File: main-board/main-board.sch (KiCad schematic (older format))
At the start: 54 parts, among them J1 MOTOR0, J10 PROGRAMMER, J11 CAM0, J12 CAM1, J13 CAM2, J14 CAM3, J15 CAM4, J16 CAM5, J17 CAM6, J18 CAM7, J2 MOTOR1, J3 MOTOR2, J4 MOTOR3, J5 RJ45, J6 MOTOR4, J7 MOTOR5, J8 MOTOR6, J9 MOTOR7, SW1 SW_SPST, T1 ATB2012E-50011M-T01, T2 ATB2012E-50011M-T01, U1 MCP2515-EST, U2 ATA6560, U3 ATmega2560-16AU | Main Proc, U4 MC14051B, U5 MC14051B, U6 SN75HVD3082EDR, U7 LTC1983ES6-5-TRPBF, U8 OPAMP, U9 OPAMP, Y1 20MHz, Y2 20MHz

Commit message: begin board
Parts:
- added J19: PowerBoard Interface, Connector_JST:JST_EH_B04B-EH-A_1x04_P2.50mm_Vertical, symbol Connector:Conn_01x04_Male
- added J20: IMU Breakout, Connector_JST:JST_EH_B04B-EH-A_1x04_P2.50mm_Vertical, symbol Connector:Conn_01x04_Male
- C1, C2, C3, C4, C5, C6, C7, C8, C9: footprint (none) -> Capacitor_SMD:C_0603_1608Metric
- D1: footprint (none) -> Diode_SMD:D_0603_1608Metric
- D2: footprint SOT-23-3 -> Package_TO_SOT_SMD:SOT-23
- J1, J2, J3, J4, J6, J7, J8, J9: footprint (none) -> Connector_JST:JST_EH_B03B-EH-A_1x03_P2.50mm_Vertical
- J10: footprint (none) -> Connector_JST:JST_EH_B05B-EH-A_1x05_P2.50mm_Vertical
- J11, J12, J13, J14, J15, J16, J17, J18: footprint (none) -> Connector_PinSocket_2.54mm:PinSocket_2x03_P2.54mm_Vertical
- J5: footprint (none) -> Connector_RJ:RJ45_Amphenol_54602-x08_Horizontal
- R1, R10, R11, R2, R3, R4, R5, R6, R7, R8, R9: footprint (none) -> Resistor_SMD:R_0603_1608Metric
- SW1: footprint (none) -> Button_Switch_THT:SW_Tactile_Straight_KSA0Axx1LFTR
- T1, T2: footprint XFMR_ATB2012E-50011M-T01 -> HHM1595A1:BALUN_HHM1595A1
- U2: footprint (none) -> Package_SO:SOIC-8_3.9x4.9mm_P1.27mm
- U4, U5: footprint (none) -> Package_SO:SOIC-16_3.9x9.9mm_P1.27mm
- U6: footprint D8 -> Package_SO:SOIC-8_3.9x4.9mm_P1.27mm
- U7: footprint SOT-23_S6 -> Package_TO_SOT_SMD:SOT-23-6
- U8, U9: footprint (none) -> Package_TO_SOT_SMD:SOT-23-5
- Y1, Y2: footprint (none) -> Crystal:Crystal_HC49-U_Vertical
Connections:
- net labels added: +3V3, SCL, SDA
- wire segments 140 -> 141
- no-connect marks 67 -> 65

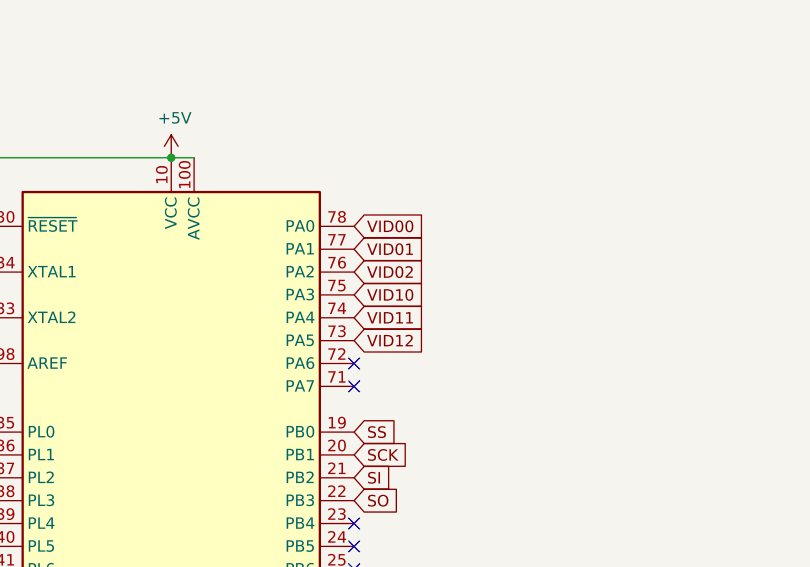
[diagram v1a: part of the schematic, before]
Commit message: add traces for all signals except cameras
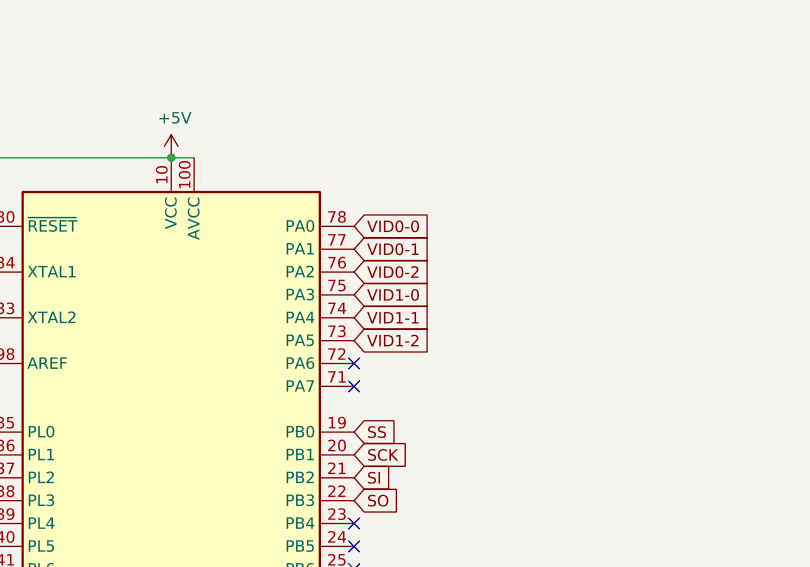
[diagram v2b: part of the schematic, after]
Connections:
- net labels removed: VID00, VID01, VID02, VID10, VID11, VID12
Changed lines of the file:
@@
 $EndComp
 Text GLabel 6300 1650 2    50   Input ~ 0
-VID00
+VID0-0
 Text GLabel 6300 1750 2    50   Input ~ 0
-VID01
+VID0-1
 Text GLabel 6300 1850 2    50   Input ~ 0
-VID02
+VID0-2
 Text GLabel 6300 1950 2    50   Input ~ 0
-VID10
+VID1-0
 Text GLabel 6300 2050 2    50   Input ~ 0
-VID11
+VID1-1
 Text GLabel 6300 2150 2    50   Input ~ 0
-VID12
+VID1-2
 Text GLabel 4700 6650 0    50   Input ~ 0
 M0

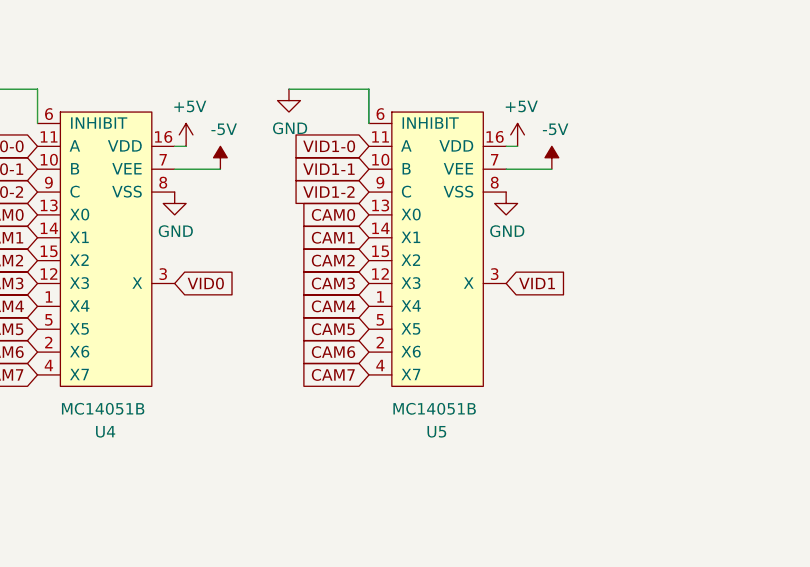
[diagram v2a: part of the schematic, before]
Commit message: complete electrical circuit, needs holes
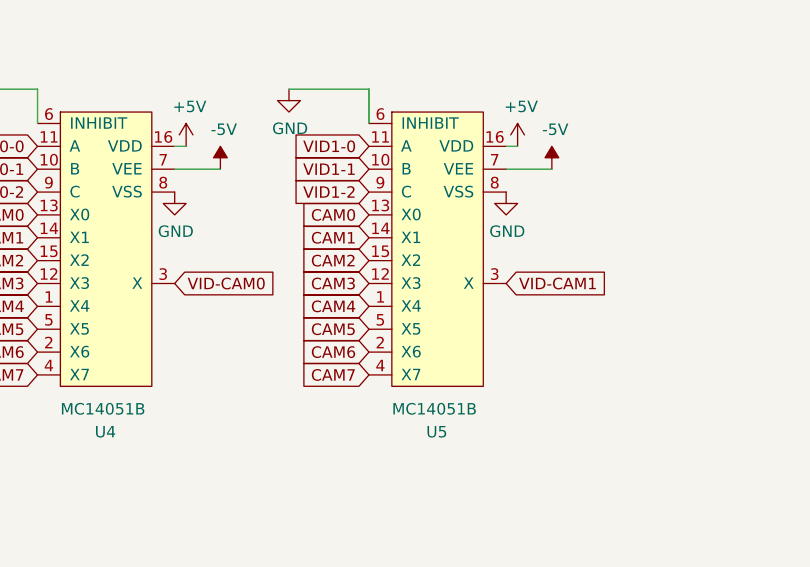
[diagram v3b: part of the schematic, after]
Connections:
- net labels removed: VID0, VID1
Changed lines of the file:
@@
 $EndComp
 Text GLabel 9650 3400 2    50   Input ~ 0
-VID0
+VID-CAM0
 Text GLabel 11100 3400 2    50   Input ~ 0
-VID1
+VID-CAM1
 $Comp
 L power:GND #PWR034

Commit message: Review+changes- see description
Schematic:
* add ICSP connector
* add VPP and diode D3for uC programming


PCB:
* add ICSP connector
* add VPP diode
* change tether connector from RJ45 to 2.54mm pitch 1x8 header
* slight silkscreen changes
* removed some overlapping vias
* moved vias from SMD pads
* slight changes to GND top copper pour



Requested before approval:
* silkscreen work
* Vinnie review


Requested other:
* Schematic formatting- boxes, labels, page layout, etc
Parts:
- added D3: D_x2_KCom_AAK, Package_TO_SOT_SMD:SOT-23, symbol Device:D_x2_KCom_AAK
- added J21: ICSP (DO NOT POPULATE), Connector_PinHeader_1.00mm:PinHeader_2x03_P1.00mm_Vertical, symbol Connector_Generic:Conn_02x03_Odd_Even
- D2: symbol CDSOT23-SM712:CDSOT23-SM712 -> main-board-rescue:CDSOT23-SM712-CDSOT23-SM712
- J5: footprint Connector_RJ:RJ45_Amphenol_54602-x08_Horizontal -> Connector_PinHeader_2.54mm:PinHeader_1x08_P2.54mm_Vertical
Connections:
- net labels added: RESET_MAIN, VPP
- wire segments 141 -> 151
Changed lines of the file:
@@
 F 0 "J5" V 8659 9330 50  0000 L CNN
 F 1 "RJ45" V 8750 9330 50  0000 L CNN
-F 2 "Connector_RJ:RJ45_Amphenol_54602-x08_Horizontal" V 8650 8825 50  0001 C CNN
+F 2 "Connector_PinHeader_2.54mm:PinHeader_1x08_P2.54mm_Vertical" V 8650 8825 50  0001 C CNN
 F 3 "~" V 8650 8825 50  0001 C CNN
 	1    8650 8800
@@
 L power:+5V #PWR012
 U 1 1 5BC811BE
-P 5500 1350
-F 0 "#PWR012" H 5500 1200 50  0001 C CNN
-F 1 "+5V" H 5515 1523 50  0000 C CNN
-F 2 "" H 5500 1350 50  0001 C CNN
-F 3 "" H 5500 1350 50  0001 C CNN
-	1    5500 1350
-	1    0    0    -1
-$EndComp
-Wire Wire Line
-	5500 1350 5600 1350
+P 5950 1050
+F 0 "#PWR012" H 5950 900 50  0001 C CNN
+F 1 "+5V" H 5965 1223 50  0000 C CNN
+F 2 "" H 5950 1050 50  0001 C CNN
+F 3 "" H 5950 1050 50  0001 C CNN
+	1    5950 1050
+	1    0    0    -1
+$EndComp
+Wire Wire Line
+	5500 1350 5550 1350
 Connection ~ 5500 1350
 $Comp
@@
 F 3 "" H 10650 8300 50  0001 C CNN
 	1    10650 8300
-	1    0    0    -1
-$EndComp
-$Comp
-L power:+5V #PWR039
-U 1 1 5BCA444A
-P 10650 7900
-F 0 "#PWR039" H 10650 7750 50  0001 C CNN
-F 1 "+5V" H 10665 8073 50  0000 C CNN
-F 2 "" H 10650 7900 50  0001 C CNN
-F 3 "" H 10650 7900 50  0001 C CNN
-	1    10650 7900
 	1    0    0    -1
 $EndComp
@@
 	3500 2200 3500 2300
 $Comp
-L CDSOT23-SM712:CDSOT23-SM712 D2
+L main-board-rescue:CDSOT23-SM712-CDSOT23-SM712 D2
 U 1 1 5BCEE3C3
 P 14800 1500
@@
 SDA
 NoConn ~ 6300 4750
+$Comp
+L Connector_Generic:Conn_02x03_Odd_Even J21
+U 1 1 5BD727D5
+P 10900 10000
+F 0 "J21" H 10950 10350 50  0000 C CNN
+F 1 "ICSP (DO NOT POPULATE)" H 10600 10250 50  0000 C CNN
+F 2 "Connector_PinHeader_1.00mm:PinHeader_2x03_P1.00mm_Vertical" H 10900 10000 50  0001 C CNN
+F 3 "~" H 10900 10000 50  0001 C CNN
+	1    10900 10000
+	1    0    0    -1
+$EndComp
+Text GLabel 10700 9900 0    50   Input ~ 0
+SO
+Text GLabel 11200 10000 2    50   Input ~ 0
+SI
+Text GLabel 10700 10000 0    50   Input ~ 0
+SCK
+Text GLabel 10700 10100 0    50   Input ~ 0
+RESET_MAIN
+$Comp
+L power:GND #PWR0105
+U 1 1 5BD754CF
+P 11250 10150
+F 0 "#PWR0105" H 11250 9900 50  0001 C CNN
+F 1 "GND" H 11255 9977 50  0000 C CNN
+F 2 "" H 11250 10150 50  0001 C CNN
+F 3 "" H 11250 10150 50  0001 C CNN
+	1    11250 10150
+	1    0    0    -1
+$EndComp
+Wire Wire Line
+	11250 10150 11250 10100
+Wire Wire Line
+	11250 10100 11200 10100
+Wire Wire Line
+	11200 9900 11250 9900
+Wire Wire Line
+	11250 9900 11250 9850
+$Comp
+L Device:D_x2_KCom_AAK D3
+U 1 1 5BD83587
+P 5550 1100
+F 0 "D3" H 5550 1316 50  0000 C CNN
+F 1 "D_x2_KCom_AAK" H 5550 1225 50  0000 C CNN
+F 2 "Package_TO_SOT_SMD:SOT-23" H 5550 1100 50  0001 C CNN
+F 3 "~" H 5550 1100 50  0001 C CNN
+	1    5550 1100
+	1    0    0    -1
+$EndComp
+Wire Wire Line
+	5950 1050 5950 1100
+Wire Wire Line
+	5950 1100 5850 1100
+$Comp
+L power:VPP #PWR0106
+U 1 1 5BD8A805
+P 5150 1050
+F 0 "#PWR0106" H 5150 900 50  0001 C CNN
+F 1 "VPP" H 5165 1223 50  0000 C CNN
+F 2 "" H 5150 1050 50  0001 C CNN
+F 3 "" H 5150 1050 50  0001 C CNN
+	1    5150 1050
+	1    0    0    -1
+$EndComp
+Wire Wire Line
+	5250 1100 5150 1100
+Wire Wire Line
+	5150 1100 5150 1050
+Wire Wire Line
+	5550 1300 5550 1350
+Connection ~ 5550 1350
+Wire Wire Line
+	5550 1350 5600 1350
+$Comp
+L power:VPP #PWR0107
+U 1 1 5BDA353F
+P 11250 9850
+F 0 "#PWR0107" H 11250 9700 50  0001 C CNN
+F 1 "VPP" H 11265 10023 50  0000 C CNN
+F 2 "" H 11250 9850 50  0001 C CNN
+F 3 "" H 11250 9850 50  0001 C CNN
+	1    11250 9850
+	1    0    0    -1
+$EndComp
+$Comp
+L power:VPP #PWR0108
+U 1 1 5BDA39A3
+P 10650 7900
+F 0 "#PWR0108" H 10650 7750 50  0001 C CNN
+F 1 "VPP" H 10665 8073 50  0000 C CNN
+F 2 "" H 10650 7900 50  0001 C CNN
+F 3 "" H 10650 7900 50  0001 C CNN
+	1    10650 7900
+	1    0    0    -1
+$EndComp
 $EndSCHEMATC

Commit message: Various changes (see description)
Schematic Changes:
* add optional second RS485
* add filter caps to IC power
* remove input resistor on reset line of 2560
* change CAN UART lines to be tx<>tx rx<>rx

PCB Changes:
* reorganize camera section
* add header labels
* minor fixes
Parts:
- removed C7: 10uF, Capacitor_SMD:C_0603_1608Metric, symbol Device:C_Small
- removed J11: CAM0, Connector_PinSocket_2.54mm:PinSocket_2x03_P2.54mm_Vertical, symbol Connector_Generic:Conn_02x03_Counter_Clockwise
- removed J12: CAM1, Connector_PinSocket_2.54mm:PinSocket_2x03_P2.54mm_Vertical, symbol Connector_Generic:Conn_02x03_Counter_Clockwise
- removed J13: CAM2, Connector_PinSocket_2.54mm:PinSocket_2x03_P2.54mm_Vertical, symbol Connector_Generic:Conn_02x03_Counter_Clockwise
- removed J14: CAM3, Connector_PinSocket_2.54mm:PinSocket_2x03_P2.54mm_Vertical, symbol Connector_Generic:Conn_02x03_Counter_Clockwise
- removed J15: CAM4, Connector_PinSocket_2.54mm:PinSocket_2x03_P2.54mm_Vertical, symbol Connector_Generic:Conn_02x03_Counter_Clockwise
- removed J16: CAM5, Connector_PinSocket_2.54mm:PinSocket_2x03_P2.54mm_Vertical, symbol Connector_Generic:Conn_02x03_Counter_Clockwise
- removed J17: CAM6, Connector_PinSocket_2.54mm:PinSocket_2x03_P2.54mm_Vertical, symbol Connector_Generic:Conn_02x03_Counter_Clockwise
- removed J18: CAM7, Connector_PinSocket_2.54mm:PinSocket_2x03_P2.54mm_Vertical, symbol Connector_Generic:Conn_02x03_Counter_Clockwise
- removed U8, U9: OPAMP, Package_TO_SOT_SMD:SOT-23-5, symbol pspice:OPAMP
- added C10, C11, C12, C13, C14, C15, C16, C17, C18, C19: 100nF, Capacitor_SMD:C_0603_1608Metric, symbol Device:C_Small
- added D4: CDSOT23-SM712, Package_TO_SOT_SMD:SOT-23, symbol main-board-rescue:CDSOT23-SM712-CDSOT23-SM712
- added J11: CAM0, symbol Connector_Generic:Conn_02x03_Odd_Even
- added J12: CAM1, symbol Connector_Generic:Conn_02x03_Odd_Even
- added J13: CAM2, symbol Connector_Generic:Conn_02x03_Odd_Even
- added J14: CAM3, symbol Connector_Generic:Conn_02x03_Odd_Even
- added J15: CAM4, symbol Connector_Generic:Conn_02x03_Odd_Even
- added J16: CAM5, symbol Connector_Generic:Conn_02x03_Odd_Even
- added J17: CAM6, symbol Connector_Generic:Conn_02x03_Odd_Even
- added J18: CAM7, symbol Connector_Generic:Conn_02x03_Odd_Even
- added R12: 10k, Resistor_SMD:R_0603_1608Metric, symbol Device:R_Small
- added R13, R14: 10, Resistor_SMD:R_0603_1608Metric, symbol Device:R_Small
- added R15, R16: 100, Resistor_SMD:R_0603_1608Metric, symbol Device:R_Small
- added U8: THS7314DR, ths7314dr:THS7314DR, symbol ths7314dr:THS7314DR
- added U9: SN75HVD3082EDR, Package_SO:SOIC-8_3.9x4.9mm_P1.27mm, symbol main-board-rescue:SN75HVD3082EDR-SN75HVD3082EDR_
- J1, J2, J3, J4, J6, J7, J8, J9: footprint Connector_JST:JST_EH_B03B-EH-A_1x03_P2.50mm_Vertical -> Connector_PinHeader_2.54mm:PinHeader_1x03_P2.54mm_Vertical
- J10: footprint Connector_JST:JST_EH_B05B-EH-A_1x05_P2.50mm_Vertical -> Connector_PinHeader_2.54mm:PinHeader_1x05_P2.54mm_Vertical
- J19, J20: footprint Connector_JST:JST_EH_B04B-EH-A_1x04_P2.50mm_Vertical -> Connector_PinHeader_2.54mm:PinHeader_1x04_P2.54mm_Vertical
- R5: value 100k -> 10k
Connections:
- net labels added: RS485+2, RS485-2
- wire segments 151 -> 200
- no-connect marks 65 -> 68
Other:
- note added: "SECOND RS485 TRANSCEIVER IN CASE FULL DUPLEX IS MORE IMPORTANT THAN CAN"
- moved on the sheet: C1, C2, C3, C4, C5, C6, C8, C9, D1, D2, D3, J1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

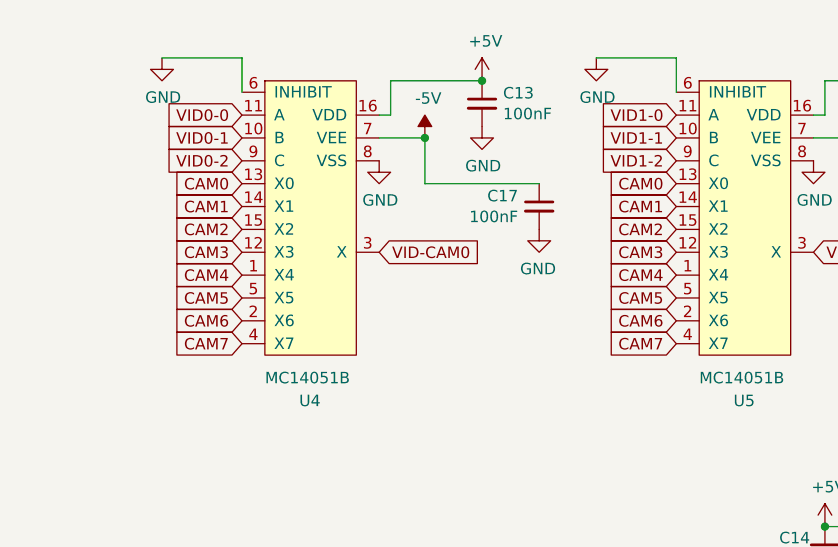
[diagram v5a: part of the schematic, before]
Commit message: S1.0.1 B1.0.1 See Desc
* Reorganized video and motor connectors for easier ROV wiring

* PCB Via redesign
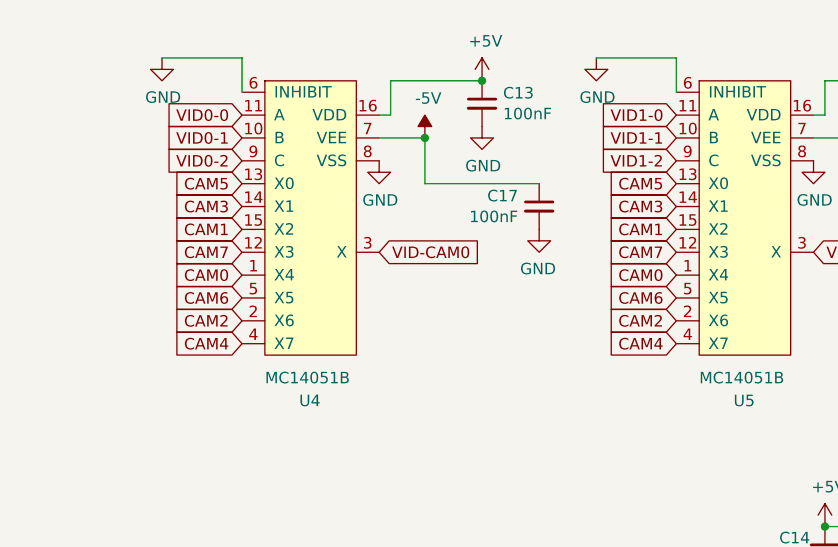
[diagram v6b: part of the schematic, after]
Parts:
- J11, J12, J13, J14, J15, J16, J17, J18: footprint (none) -> Connector_PinHeader_2.54mm:PinHeader_2x03_P2.54mm_Vertical
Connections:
- net CAM0: now also U4.1 (X4), U5.1 (X4); no longer U4.13 (X0), U5.13 (X0)
- net CAM1: now also U4.15 (X2), U5.15 (X2); no longer U4.14 (X1), U5.14 (X1)
- net CAM2: now also U4.2 (X6), U5.2 (X6); no longer U4.15 (X2), U5.15 (X2)
- net CAM3: now also U4.14 (X1), U5.14 (X1); no longer U4.12 (X3), U5.12 (X3)
- net CAM4: now also U4.4 (X7), U5.4 (X7); no longer U4.1 (X4), U5.1 (X4)
- net CAM5: now also U4.13 (X0), U5.13 (X0); no longer U4.5 (X5), U5.5 (X5)
- net CAM6: now also U4.5 (X5), U5.5 (X5); no longer U4.2 (X6), U5.2 (X6)
- net CAM7: now also U4.12 (X3), U5.12 (X3); no longer U4.4 (X7), U5.4 (X7)
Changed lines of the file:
@@
 Sheet 1 1
 Title "TITAN-II Main Board"
-Date "2018-10-31"
-Rev "1.0.0"
+Date "2018-11-01"
+Rev "1.0.1"
 Comp "Missouri University of Science and Technology - Underwater Robotics Team"
 Comment1 "The main logic board / motherboard of the TITAN-II 2018-2019 UROV"
@@
 Text GLabel 7200 1150 0    50   Input ~ 0
 VID0-2
+Text GLabel 9100 1650 0    50   Input ~ 0
+CAM0
+Text GLabel 9100 1450 0    50   Input ~ 0
+CAM1
+Text GLabel 9100 1850 0    50   Input ~ 0
+CAM2
+Text GLabel 9100 1350 0    50   Input ~ 0
+CAM3
+Text GLabel 9100 1950 0    50   Input ~ 0
+CAM4
 Text GLabel 9100 1250 0    50   Input ~ 0
-CAM0
-Text GLabel 9100 1350 0    50   Input ~ 0
-CAM1
-Text GLabel 9100 1450 0    50   Input ~ 0
-CAM2
+CAM5
+Text GLabel 9100 1750 0    50   Input ~ 0
+CAM6
 Text GLabel 9100 1550 0    50   Input ~ 0
-CAM3
-Text GLabel 9100 1650 0    50   Input ~ 0
-CAM4
-Text GLabel 9100 1750 0    50   Input ~ 0
-CAM5
-Text GLabel 9100 1850 0    50   Input ~ 0
-CAM6
-Text GLabel 9100 1950 0    50   Input ~ 0
 CAM7
-Text GLabel 7200 1950 0    50   Input ~ 0
-CAM7
-Text GLabel 7200 1850 0    50   Input ~ 0
-CAM6
-Text GLabel 7200 1750 0    50   Input ~ 0
-CAM5
-Text GLabel 7200 1650 0    50   Input ~ 0
-CAM4
-Text GLabel 7200 1550 0    50   Input ~ 0
-CAM3
-Text GLabel 7200 1450 0    50   Input ~ 0
-CAM2
-Text GLabel 7200 1350 0    50   Input ~ 0
-CAM1
-Text GLabel 7200 1250 0    50   Input ~ 0
-CAM0
 $Comp
 L power:+5V #PWR046
@@
 F 0 "J11" H 7200 5067 50  0000 C CNN
 F 1 "CAM0" H 7200 4976 50  0000 C CNN
-F 2 "" H 7150 4750 50  0001 C CNN
+F 2 "Connector_PinHeader_2.54mm:PinHeader_2x03_P2.54mm_Vertical" H 7150 4750 50  0001 C CNN
 F 3 "~" H 7150 4750 50  0001 C CNN
 	1    7150 4750
@@
 F 0 "J12" H 7200 5767 50  0000 C CNN
 F 1 "CAM1" H 7200 5676 50  0000 C CNN
-F 2 "" H 7150 5450 50  0001 C CNN
+F 2 "Connector_PinHeader_2.54mm:PinHeader_2x03_P2.54mm_Vertical" H 7150 5450 50  0001 C CNN
 F 3 "~" H 7150 5450 50  0001 C CNN
 	1    7150 5450
@@
 F 0 "J13" H 7200 6417 50  0000 C CNN
 F 1 "CAM2" H 7200 6326 50  0000 C CNN
-F 2 "" H 7150 6100 50  0001 C CNN
+F 2 "Connector_PinHeader_2.54mm:PinHeader_2x03_P2.54mm_Vertical" H 7150 6100 50  0001 C CNN
 F 3 "~" H 7150 6100 50  0001 C CNN
 	1    7150 6100
@@
 F 0 "J14" H 7200 7067 50  0000 C CNN
 F 1 "CAM3" H 7200 6976 50  0000 C CNN
-F 2 "" H 7150 6750 50  0001 C CNN
+F 2 "Connector_PinHeader_2.54mm:PinHeader_2x03_P2.54mm_Vertical" H 7150 6750 50  0001 C CNN
 F 3 "~" H 7150 6750 50  0001 C CNN
 	1    7150 6750
@@
 F 0 "J15" H 8500 5067 50  0000 C CNN
 F 1 "CAM4" H 8500 4976 50  0000 C CNN
-F 2 "" H 8450 4750 50  0001 C CNN
+F 2 "Connector_PinHeader_2.54mm:PinHeader_2x03_P2.54mm_Vertical" H 8450 4750 50  0001 C CNN
 F 3 "~" H 8450 4750 50  0001 C CNN
 	1    8450 4750
@@
 F 0 "J16" H 8500 5767 50  0000 C CNN
 F 1 "CAM5" H 8500 5676 50  0000 C CNN
-F 2 "" H 8450 5450 50  0001 C CNN
+F 2 "Connector_PinHeader_2.54mm:PinHeader_2x03_P2.54mm_Vertical" H 8450 5450 50  0001 C CNN
 F 3 "~" H 8450 5450 50  0001 C CNN
 	1    8450 5450
@@
 F 0 "J17" H 8500 6417 50  0000 C CNN
 F 1 "CAM6" H 8500 6326 50  0000 C CNN
-F 2 "" H 8450 6100 50  0001 C CNN
+F 2 "Connector_PinHeader_2.54mm:PinHeader_2x03_P2.54mm_Vertical" H 8450 6100 50  0001 C CNN
 F 3 "~" H 8450 6100 50  0001 C CNN
 	1    8450 6100
@@
 F 0 "J18" H 8500 7067 50  0000 C CNN
 F 1 "CAM7" H 8500 6976 50  0000 C CNN
-F 2 "" H 8450 6750 50  0001 C CNN
+F 2 "Connector_PinHeader_2.54mm:PinHeader_2x03_P2.54mm_Vertical" H 8450 6750 50  0001 C CNN
 F 3 "~" H 8450 6750 50  0001 C CNN
 	1    8450 6750
 	1    0    0    -1
 $EndComp
+Text GLabel 7200 1650 0    50   Input ~ 0
+CAM0
+Text GLabel 7200 1450 0    50   Input ~ 0
+CAM1
+Text GLabel 7200 1850 0    50   Input ~ 0
+CAM2
+Text GLabel 7200 1350 0    50   Input ~ 0
+CAM3
+Text GLabel 7200 1950 0    50   Input ~ 0
+CAM4
+Text GLabel 7200 1250 0    50   Input ~ 0
+CAM5
+Text GLabel 7200 1750 0    50   Input ~ 0
+CAM6
+Text GLabel 7200 1550 0    50   Input ~ 0
+CAM7
 $EndSCHEMATC
